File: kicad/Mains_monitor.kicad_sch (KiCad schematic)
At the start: 35 parts, among them J1 Screw_Terminal_01x02, J2 Screw_Terminal_01x02, K1 SANYOU_SRD_Form_C, Q1 NPN, U1 HLW8032

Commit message: Update footprints and git ignore
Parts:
- removed JP1: RELAY LOGIC BYPASS, Jumper:SolderJumper-2_P1.3mm_Open_RoundedPad1.0x1.5mm, symbol Jumper:SolderJumper_2_Open
- C2, C3, C6: footprint Capacitor_THT:C_Radial_D5.0mm_H7.0mm_P2.00mm -> Capacitor_THT:C_Rect_L4.6mm_W2.0mm_P2.50mm_MKS02_FKP02
- C4: footprint Capacitor_THT:C_Radial_D5.0mm_H7.0mm_P2.00mm -> Capacitor_THT:C_Disc_D3.0mm_W1.6mm_P2.50mm
- C5: footprint Capacitor_THT:C_Radial_D5.0mm_H7.0mm_P2.00mm -> Capacitor_THT:C_Radial_D10.0mm_H12.5mm_P5.00mm
- R1, R10, R2, R3, R4, R7, R8, R9: footprint Resistor_THT:R_Axial_DIN0207_L6.3mm_D2.5mm_P10.16mm_Horizontal -> Resistor_THT:R_Axial_DIN0207_L6.3mm_D2.5mm_P7.62mm_Horizontal
- R11, R12, R13, R14, R5, R6: footprint Resistor_THT:R_Axial_DIN0207_L6.3mm_D2.5mm_P10.16mm_Horizontal -> Resistor_THT:R_Axial_DIN0207_L6.3mm_D2.5mm_P2.54mm_Vertical
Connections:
- net RLY_CTRL: now also R1.1
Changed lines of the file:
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@@
 	(wire
 		(pts
-			(xy 191.77 66.04) (xy 201.93 66.04)
+			(xy 191.77 66.04) (xy 218.44 66.04)
 		)
 		(stroke
@@
 	(wire
 		(pts
-			(xy 209.55 66.04) (xy 218.44 66.04)
-		)
-		(stroke
-			(width 0)
-			(type default)
-		)
-	)
-	(wire
-		(pts
 			(xy 105.41 172.72) (xy 110.49 172.72)
 		)
@@
 			)
 		)
-		(property "Footprint" "Capacitor_THT:C_Radial_D5.0mm_H7.0mm_P2.00mm"
+		(property "Footprint" "Capacitor_THT:C_Rect_L4.6mm_W2.0mm_P2.50mm_MKS02_FKP02"
 			(at 87.3252 139.7 0)
 			(effects
@@
 	)
 	(symbol
-		(lib_id "Jumper:SolderJumper_2_Open")
-		(at 205.74 66.04 0)
-		(unit 1)
-		(exclude_from_sim yes)
-		(in_bom no)
-		(on_board yes)
-		(dnp no)
-		(property "Reference" "JP1"
-			(at 205.74 63.5 0)
-			(effects
-				(font
-					(size 1.27 1.27)
-				)
-			)
-		)
-		(property "Value" "RELAY LOGIC BYPASS"
-			(at 205.74 62.23 0)
-			(effects
-				(font
-					(size 1.27 1.27)
-				)
-				(hide yes)
-			)
-		)
-		(property "Footprint" "Jumper:SolderJumper-2_P1.3mm_Open_RoundedPad1.0x1.5mm"
-			(at 205.74 66.04 0)
-			(effects
-				(font
-					(size 1.27 1.27)
-				)
-				(hide yes)
-			)
-		)
-		(property "Datasheet" "~"
-			(at 205.74 66.04 0)
-			(effects
-				(font
-					(size 1.27 1.27)
-				)
-				(hide yes)
-			)
-		)
-		(property "Description" "Solder Jumper, 2-pole, open"
-			(at 205.74 66.04 0)
-			(effects
-				(font
-					(size 1.27 1.27)
-				)
-				(hide yes)
-			)
-		)
-		(pin "2"
-		)
-		(pin "1"
-		)
-		(instances
-			(project ""
-				(path "/825bfe7d-9d9b-4191-9855-e1cdfdd57fae"
-					(reference "JP1")
-					(unit 1)
-				)
-			)
-		)
-	)
-	(symbol
 		(lib_id "MCU_Module:Adafruit_Feather_HUZZAH32_ESP32")
 		(at 179.07 83.82 0)
@@
 			)
 		)
-		(property "Footprint" "Resistor_THT:R_Axial_DIN0207_L6.3mm_D2.5mm_P10.16mm_Horizontal"
+		(property "Footprint" "Resistor_THT:R_Axial_DIN0207_L6.3mm_D2.5mm_P7.62mm_Horizontal"
 			(at 76.2 150.368 90)
 			(effects
@@
 			)
 		)
-		(property "Footprint" "Resistor_THT:R_Axial_DIN0207_L6.3mm_D2.5mm_P10.16mm_Horizontal"
+		(property "Footprint" "Resistor_THT:R_Axial_DIN0207_L6.3mm_D2.5mm_P7.62mm_Horizontal"
 			(at 76.2 133.858 90)
 			(effects
@@
 			)
 		)
-		(property "Footprint" "Resistor_THT:R_Axial_DIN0207_L6.3mm_D2.5mm_P10.16mm_Horizontal"
+		(property "Footprint" "Resistor_THT:R_Axial_DIN0207_L6.3mm_D2.5mm_P2.54mm_Vertical"
 			(at 64.77 174.498 90)
 			(effects
@@
 			)
 		)
-		(property "Footprint" "Resistor_THT:R_Axial_DIN0207_L6.3mm_D2.5mm_P10.16mm_Horizontal"
+		(property "Footprint" "Resistor_THT:R_Axial_DIN0207_L6.3mm_D2.5mm_P2.54mm_Vertical"
 			(at 49.53 174.498 90)
 			(effects
@@
 			)
 		)
-		(property "Footprint" "Resistor_THT:R_Axial_DIN0207_L6.3mm_D2.5mm_P10.16mm_Horizontal"
+		(property "Footprint" "Resistor_THT:R_Axial_DIN0207_L6.3mm_D2.5mm_P7.62mm_Horizontal"
 			(at 93.218 179.07 90)
 			(effects
@@
 			)
 		)
-		(property "Footprint" "Resistor_THT:R_Axial_DIN0207_L6.3mm_D2.5mm_P10.16mm_Horizontal"
+		(property "Footprint" "Resistor_THT:R_Axial_DIN0207_L6.3mm_D2.5mm_P7.62mm_Horizontal"
 			(at 222.25 67.818 90)
 			(effects
@@
 			)
 		)
-		(property "Footprint" "Resistor_THT:R_Axial_DIN0207_L6.3mm_D2.5mm_P10.16mm_Horizontal"
+		(property "Footprint" "Resistor_THT:R_Axial_DIN0207_L6.3mm_D2.5mm_P7.62mm_Horizontal"
 			(at 101.6 174.498 90)
 			(effects
@@
 			)
 		)
-		(property "Footprint" "Capacitor_THT:C_Radial_D5.0mm_H7.0mm_P2.00mm"
+		(property "Footprint" "Capacitor_THT:C_Radial_D10.0mm_H12.5mm_P5.00mm"
 			(at 99.3648 71.12 0)
 			(effects
@@
 			)
 		)
-		(property "Footprint" "Resistor_THT:R_Axial_DIN0207_L6.3mm_D2.5mm_P10.16mm_Horizontal"
+		(property "Footprint" "Resistor_THT:R_Axial_DIN0207_L6.3mm_D2.5mm_P7.62mm_Horizontal"
 			(at 64.262 139.7 90)
 			(effects
@@
 			)
 		)
-		(property "Footprint" "Resistor_THT:R_Axial_DIN0207_L6.3mm_D2.5mm_P10.16mm_Horizontal"
+		(property "Footprint" "Resistor_THT:R_Axial_DIN0207_L6.3mm_D2.5mm_P2.54mm_Vertical"
 			(at 49.53 188.468 90)
 			(effects
@@
 			)
 		)
-		(property "Footprint" "Capacitor_THT:C_Radial_D5.0mm_H7.0mm_P2.00mm"
+		(property "Footprint" "Capacitor_THT:C_Rect_L4.6mm_W2.0mm_P2.50mm_MKS02_FKP02"
 			(at 87.3252 148.59 0)
 			(effects
@@
 			)
 		)
-		(property "Footprint" "Capacitor_THT:C_Radial_D5.0mm_H7.0mm_P2.00mm"
+		(property "Footprint" "Capacitor_THT:C_Rect_L4.6mm_W2.0mm_P2.50mm_MKS02_FKP02"
 			(at 111.4552 182.88 0)
 			(effects
@@
 			)
 		)
-		(property "Footprint" "Capacitor_THT:C_Radial_D5.0mm_H7.0mm_P2.00mm"
+		(property "Footprint" "Capacitor_THT:C_Disc_D3.0mm_W1.6mm_P2.50mm"
 			(at 93.6752 78.74 0)
 			(effects
@@
 			)
 		)
-		(property "Footprint" "Resistor_THT:R_Axial_DIN0207_L6.3mm_D2.5mm_P10.16mm_Horizontal"
+		(property "Footprint" "Resistor_THT:R_Axial_DIN0207_L6.3mm_D2.5mm_P7.62mm_Horizontal"
 			(at 132.842 105.41 90)
 			(effects
@@
 			)
 		)
-		(property "Footprint" "Resistor_THT:R_Axial_DIN0207_L6.3mm_D2.5mm_P10.16mm_Horizontal"
+		(property "Footprint" "Resistor_THT:R_Axial_DIN0207_L6.3mm_D2.5mm_P2.54mm_Vertical"
 			(at 57.15 174.498 90)
 			(effects
@@
 			)
 		)
-		(property "Footprint" "Resistor_THT:R_Axial_DIN0207_L6.3mm_D2.5mm_P10.16mm_Horizontal"
+		(property "Footprint" "Resistor_THT:R_Axial_DIN0207_L6.3mm_D2.5mm_P2.54mm_Vertical"
 			(at 57.15 188.468 90)
 			(effects
@@
 			)
 		)
-		(property "Footprint" "Resistor_THT:R_Axial_DIN0207_L6.3mm_D2.5mm_P10.16mm_Horizontal"
+		(property "Footprint" "Resistor_THT:R_Axial_DIN0207_L6.3mm_D2.5mm_P7.62mm_Horizontal"
 			(at 144.78 99.568 90)
 			(effects
@@
 			)
 		)
-		(property "Footprint" "Resistor_THT:R_Axial_DIN0207_L6.3mm_D2.5mm_P10.16mm_Horizontal"
+		(property "Footprint" "Resistor_THT:R_Axial_DIN0207_L6.3mm_D2.5mm_P2.54mm_Vertical"
 			(at 64.77 188.468 90)
 			(effects

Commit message: Added in the correct footprints
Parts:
- C5: footprint Capacitor_THT:C_Radial_D10.0mm_H12.5mm_P5.00mm -> Capacitor_THT:C_Radial_D5.0mm_H11.0mm_P2.00mm
- TR2: renamed from FL2; value choke -> ZMPT107; footprint Inductor_THT:Choke_Schaffner_RN102-04-14.0x14.0mm -> mains_mon:ZMPT107-1
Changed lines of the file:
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@@
 			)
 		)
-		(property "Footprint" "Capacitor_THT:C_Radial_D10.0mm_H12.5mm_P5.00mm"
+		(property "Footprint" "Capacitor_THT:C_Radial_D5.0mm_H11.0mm_P2.00mm"
 			(at 99.3648 71.12 0)
 			(effects
@@
 		(dnp no)
 		(fields_autoplaced yes)
-		(property "Reference" "FL2"
+		(property "Reference" "TR2"
 			(at 80.01 178.1809 90)
 			(effects
@@
 			)
 		)
-		(property "Value" "choke"
+		(property "Value" "ZMPT107"
 			(at 80.01 180.7209 90)
 			(effects
@@
 			)
 		)
-		(property "Footprint" "Inductor_THT:Choke_Schaffner_RN102-04-14.0x14.0mm"
+		(property "Footprint" "mains_mon:ZMPT107-1"
 			(at 76.2 179.07 0)
 			(effects
@@
 			)
 		)
-		(property "Datasheet" "https://www.schaffner.com/products/download/product/datasheet/rn-series-common-mode-chokes-new/"
+		(property "Datasheet" ""
 			(at 76.2 179.07 0)
 			(effects
@@
 			)
 		)
-		(property "Description" "Common mode choke, 300mA, 300VAC, 12mH, 1.1 ohm, RN-102"
+		(property "Description" ""
 			(at 76.2 179.07 0)
 			(effects
@@
 			(project "Mains_monitor"
 				(path "/825bfe7d-9d9b-4191-9855-e1cdfdd57fae"
-					(reference "FL2")
-					(unit 1)
-				)
+					(reference "TR2")
+					(unit 1)
+				)

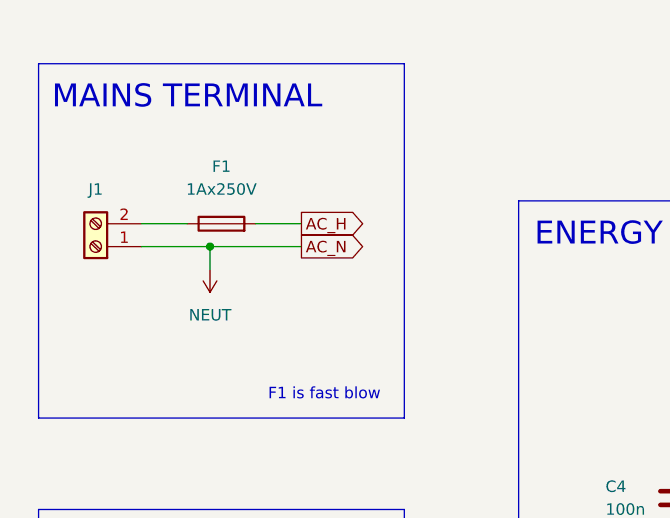
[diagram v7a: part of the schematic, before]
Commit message: added updated screw terminal footprints
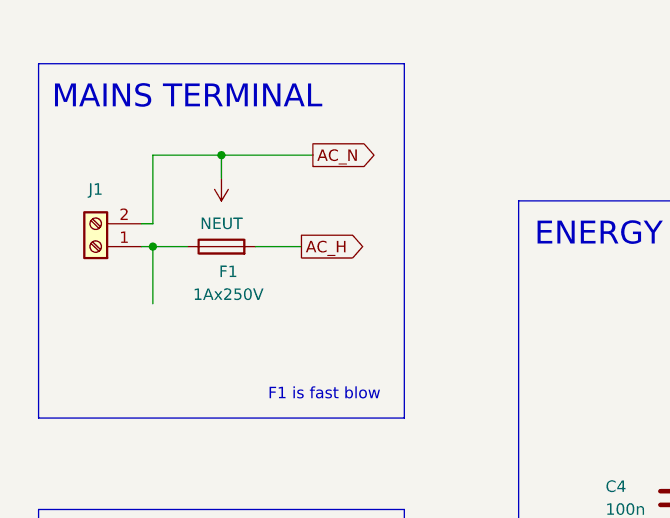
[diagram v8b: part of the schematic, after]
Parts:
- J1, J2: footprint Connector_Screw_Terminal:CONN2_020000_WED -> TerminalBlock_Phoenix:TerminalBlock_Phoenix_MKDS-1,5-2_1x02_P5.00mm_Horizontal
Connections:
- net NEUT: now also J1.2 (Pin_2); no longer J1.1 (Pin_1)
- net at F1.1: now also J1.1 (Pin_1); no longer J1.2 (Pin_2)
